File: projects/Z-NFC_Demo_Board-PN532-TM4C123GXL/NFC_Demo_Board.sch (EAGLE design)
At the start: 3 parts, among them IC1 EK-TM4C123GXLP

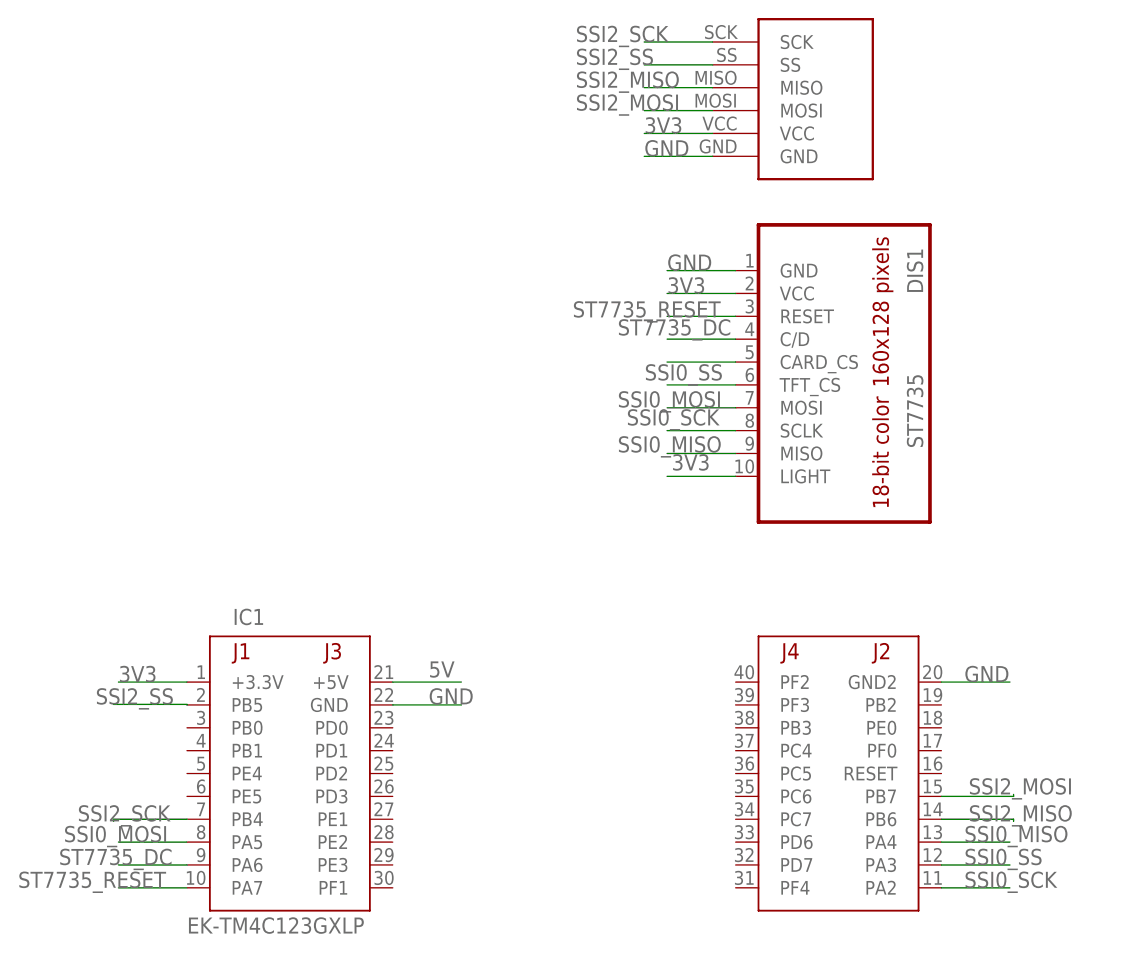
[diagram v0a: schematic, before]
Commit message: add 2 new designs of UTexas EE445M front LiDAR board
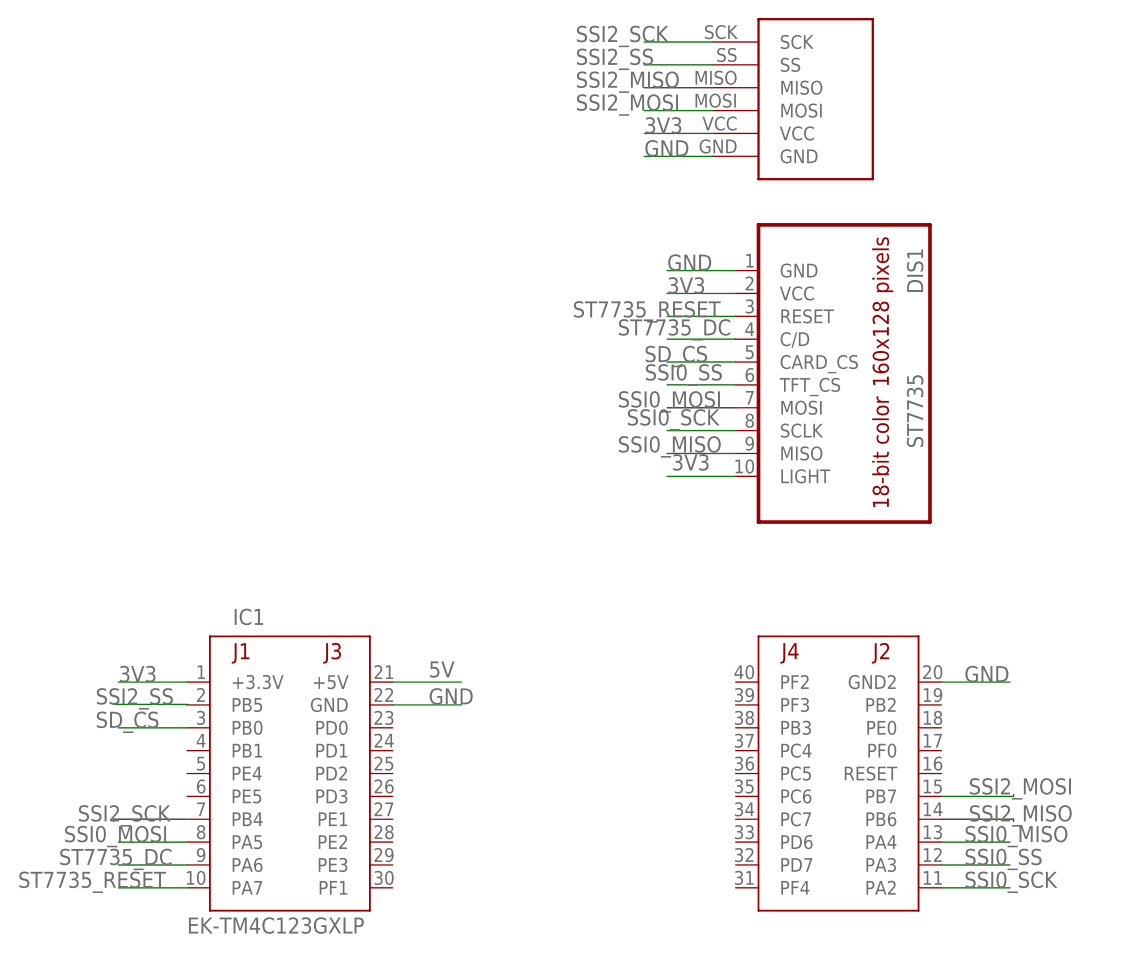
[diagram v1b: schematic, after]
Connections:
- removed net N$11: DIS1.CARD_CS
- new net SD_CS: DIS1.CARD_CS, IC1.PB0
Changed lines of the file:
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@@
-</segment>
-</net>
-<net name="N$11" class="0">
-<segment>
-<wire x1="71.12" y1="66.04" x2="63.5" y2="66.04" width="0.1524" layer="91"/>
-<pinref part="DIS1" gate="A" pin="CARD_CS"/>
 </segment>
 </net>
@@
 </segment>
 </net>
+<net name="SD_CS" class="0">
+<segment>
+<pinref part="IC1" gate="G$1" pin="PB0"/>
+<wire x1="10.16" y1="25.4" x2="2.54" y2="25.4" width="0.1524" layer="91"/>
+<label x="0" y="25.4" size="1.778" layer="95"/>
+</segment>
+<segment>
+<wire x1="71.12" y1="66.04" x2="63.5" y2="66.04" width="0.1524" layer="91"/>
+<pinref part="DIS1" gate="A" pin="CARD_CS"/>
+<label x="60.96" y="66.04" size="1.778" layer="95"/>
+</segment>
+</net>
